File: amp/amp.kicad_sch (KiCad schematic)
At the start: 82 parts, among them J1 HI Input, J2 Speaker 8Ω, J3 Headphones, J4 LO Input, J6 FX Send, J7 FX Return, Q1 S8050, SW1 PWR, SW2 FX Enable/Bypass, U1 TL074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

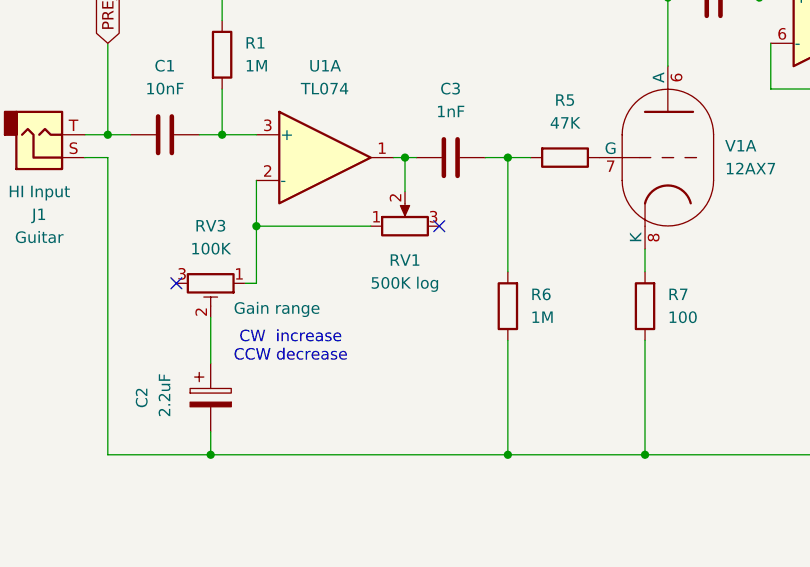
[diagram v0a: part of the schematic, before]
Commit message: Fix input opamp gain pot type (log->lin) (#38)
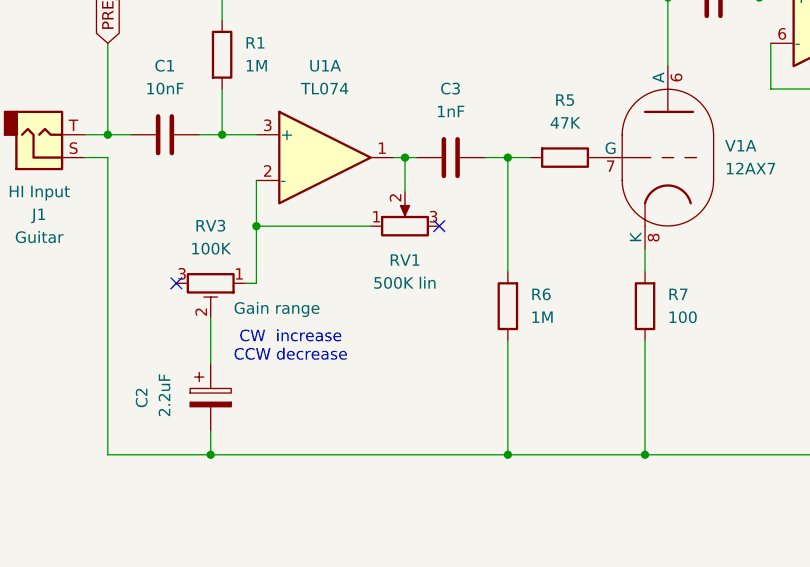
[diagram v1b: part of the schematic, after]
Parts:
- RV1: value 500K log -> 500K lin
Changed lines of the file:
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@@
 			)
 		)
-		(property "Value" "500K log"
+		(property "Value" "500K lin"
 			(at 71.12 165.1 90)
 			(effects

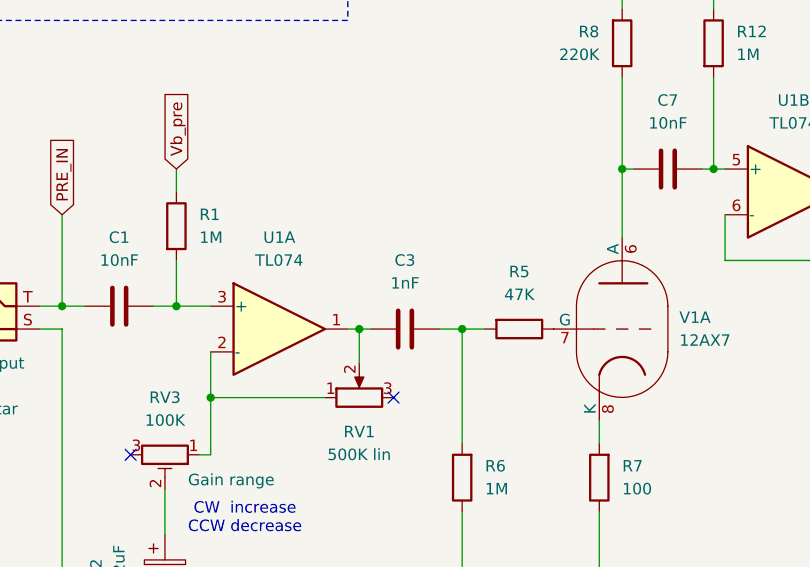
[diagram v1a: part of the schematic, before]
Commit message: u1a out coupling pot 1->10nF
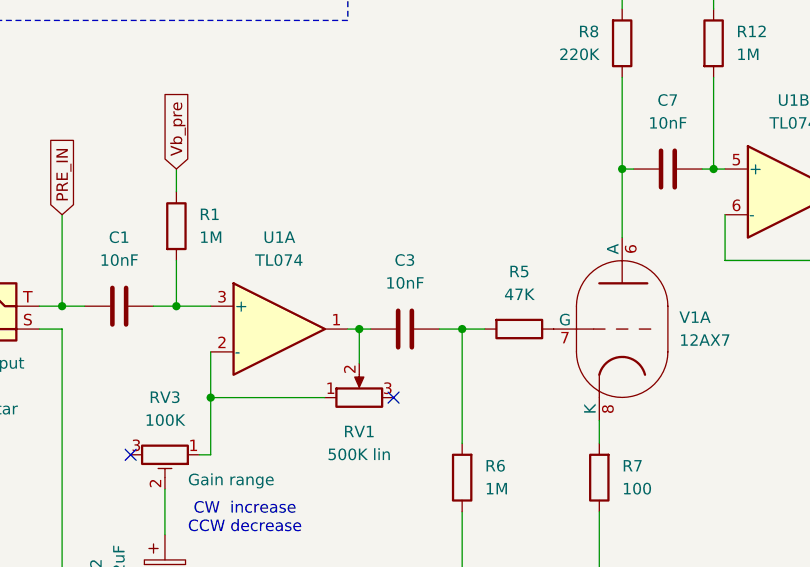
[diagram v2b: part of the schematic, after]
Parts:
- C3: value 1nF -> 10nF
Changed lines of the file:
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@@
 			)
 		)
-		(property "Value" "1nF"
+		(property "Value" "10nF"
 			(at 76.2 146.05 90)
 			(effects

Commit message: Move opamp bias source to power section
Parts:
- removed C16, C26: 10nF, symbol Device:C
- removed C25, C4: 10uF, symbol Device:C_Polarized
- removed R13, R24, R3, R4: 10K, symbol Device:R
- removed RV4, RV5: 10k, symbol Device:R_Potentiometer_Trim
- added C22: 10uF, symbol Device:C_Polarized
- added C23: 10nF, symbol Device:C
- added R22, R36: 10K, symbol Device:R
- added RV6: 10k, symbol Device:R_Potentiometer_Trim
- C14: value 100nF -> 10nF
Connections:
- net Vb_pre is gone; now on net V_{bias}: R1.1, R12.1, R14.1, R23.2
- net GND: now also R36.2
- net VCC: now also R22.2
- net Vb_mix renamed V_{bias}
- net V_{bias}: now also C22.1, C22.2, C23.1, C23.2, R22.1, RV6.2
- new net: R36.1, RV6.1
- no-connect marks 14 -> 13
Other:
- moved on the sheet: C14, C15, C6, R23, U1E, U6B

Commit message: Replace 2xNE5532 with 1xTL074
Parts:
- removed U5, U6: NE5532, symbol Amplifier_Operational:NE5532
- added C24: 10nF, symbol Device:C
- added U7: TL074, symbol Amplifier_Operational:TL074
- C27: value 1uF -> 10uF
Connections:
- net GND: now also C24.1, U7.11 (V-)
- net VCC: now also C24.2, U7.4 (V+)
- net V_{bias}: now also U7.10 (+), U7.12 (+), U7.3 (+), U7.5 (+)
- net at R32.2, R33.1, R34.1: now also U7.9 (-)
- net at C30.1, R31.1: now also U7.7
- net at R29.1, R30.1, R31.2: now also U7.6 (-)
- net at C31.1, R26.1: now also U7.1
- net at R26.2, R27.1, R28.1: now also U7.2 (-)
- net at C32.1, R32.1: now also U7.8
- new net: U7.13 (-), U7.14

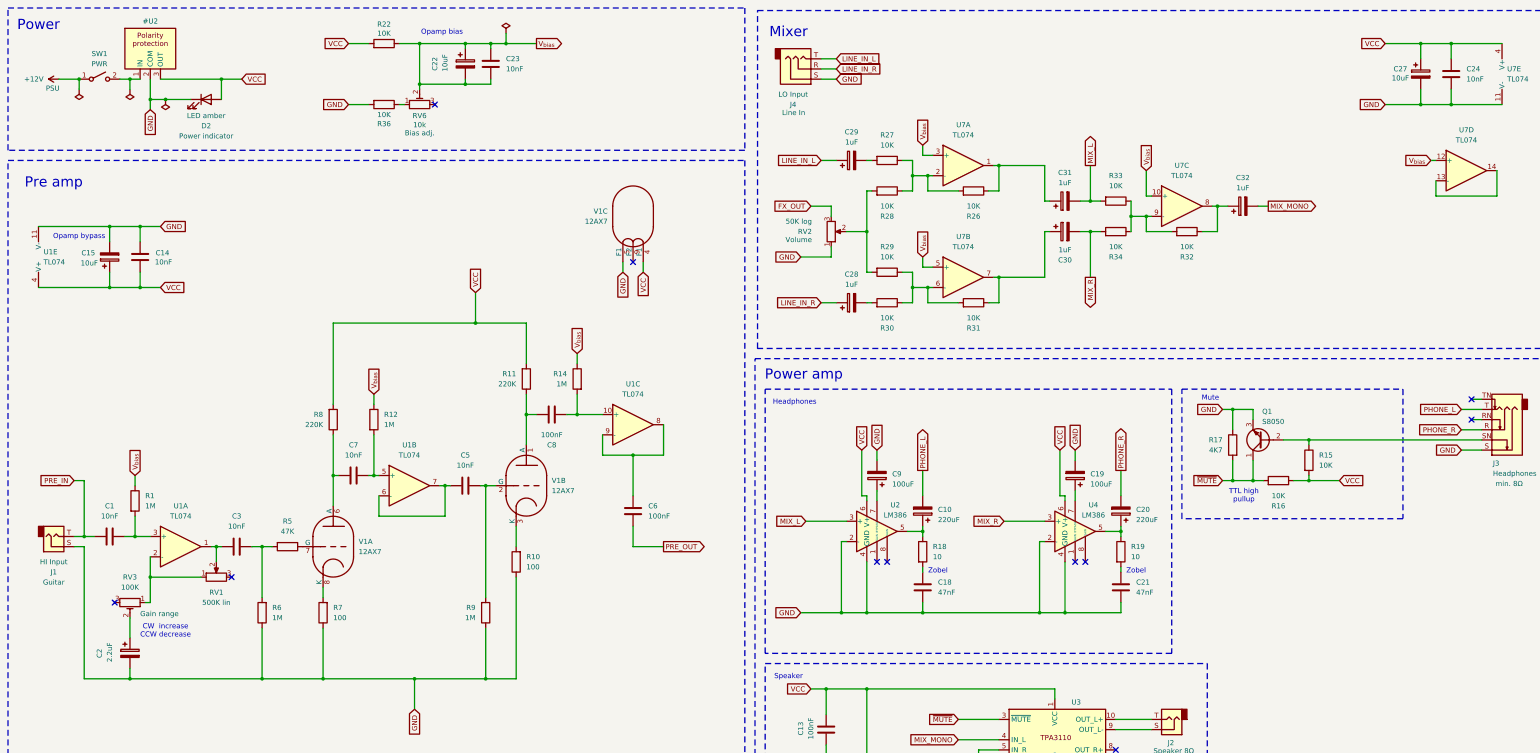
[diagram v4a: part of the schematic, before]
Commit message: Improve tube biasing (#49)
Try out Tube Cricket style tube biasing

https://beavisaudio.com/projects/TubeCricket/
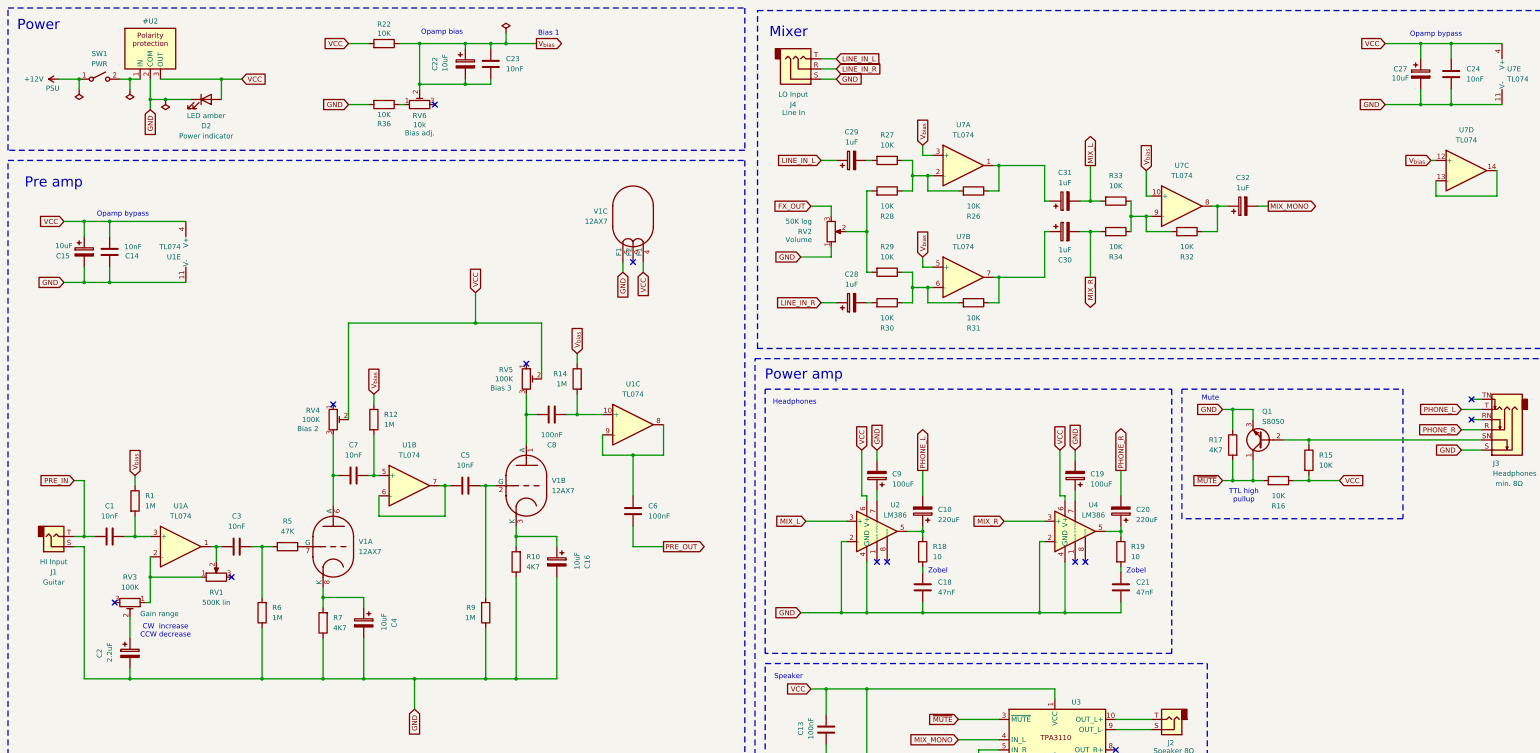
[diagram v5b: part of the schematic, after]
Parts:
- removed R11, R8: 220K, symbol Device:R
- added C16, C4: 10uF, symbol Device:C_Polarized
- added RV4, RV5: 100K, symbol Device:R_Potentiometer_Trim
- R10, R7: value 100 -> 4K7
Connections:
- net GND: now also C16.2, C4.2
- net VCC: now also RV4.2, RV5.2
- net at C8.1, V1.1 (A): now also RV5.3
- net at R7.2, V1.8 (K): now also C4.1
- net at R10.2, V1.3 (K): now also C16.1
- net at C7.1, V1.6 (A): now also RV4.3
- no-connect marks 13 -> 15
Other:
- note added: "Bias 1"
- moved on the sheet: C14, C15, R7, U1E

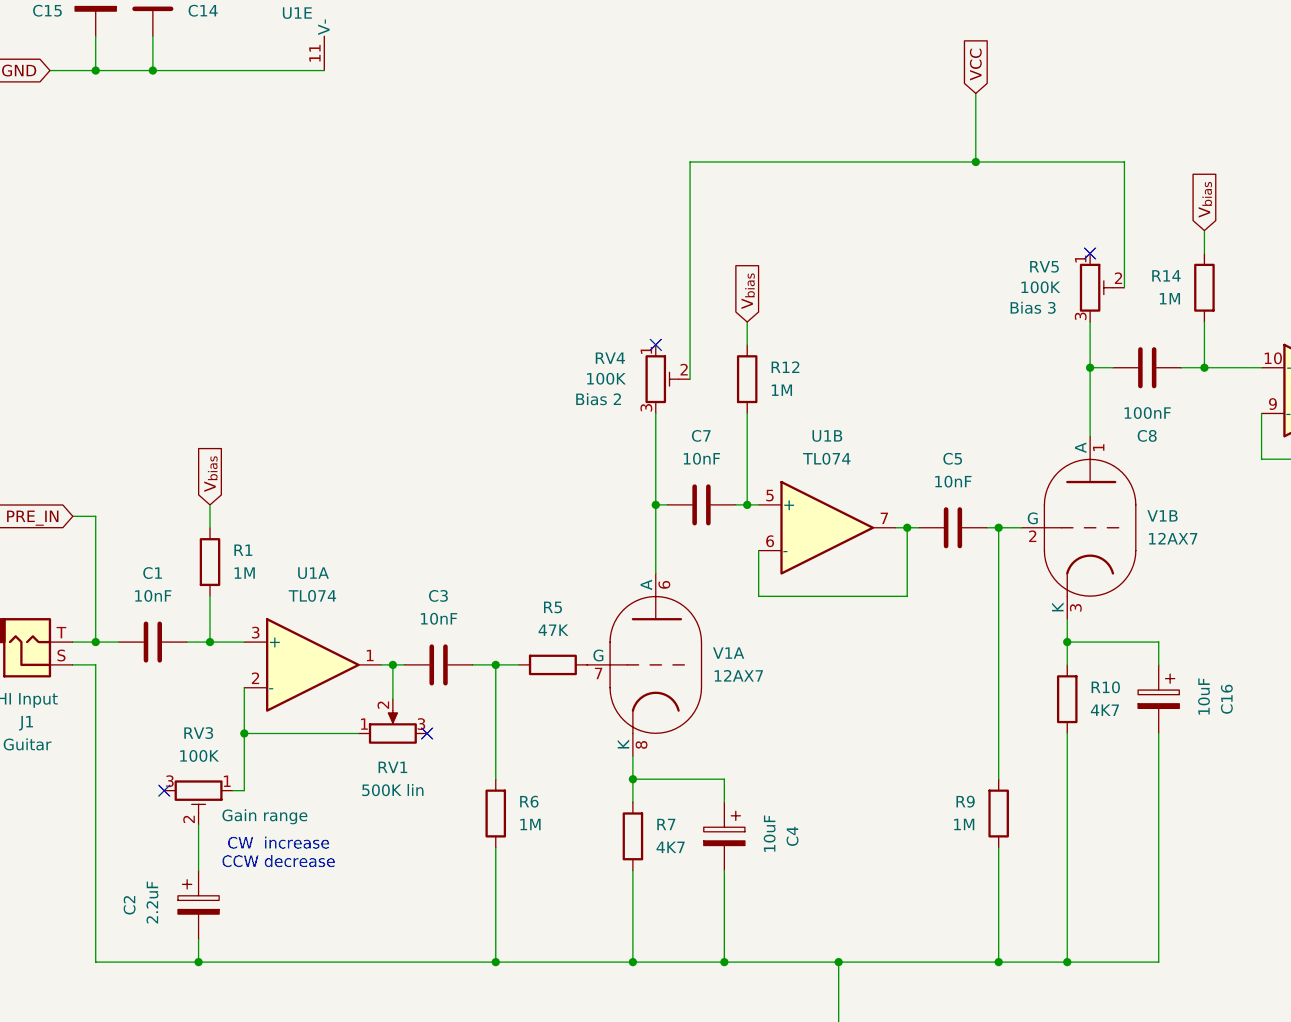
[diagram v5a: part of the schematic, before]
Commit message: Fix tube biasing
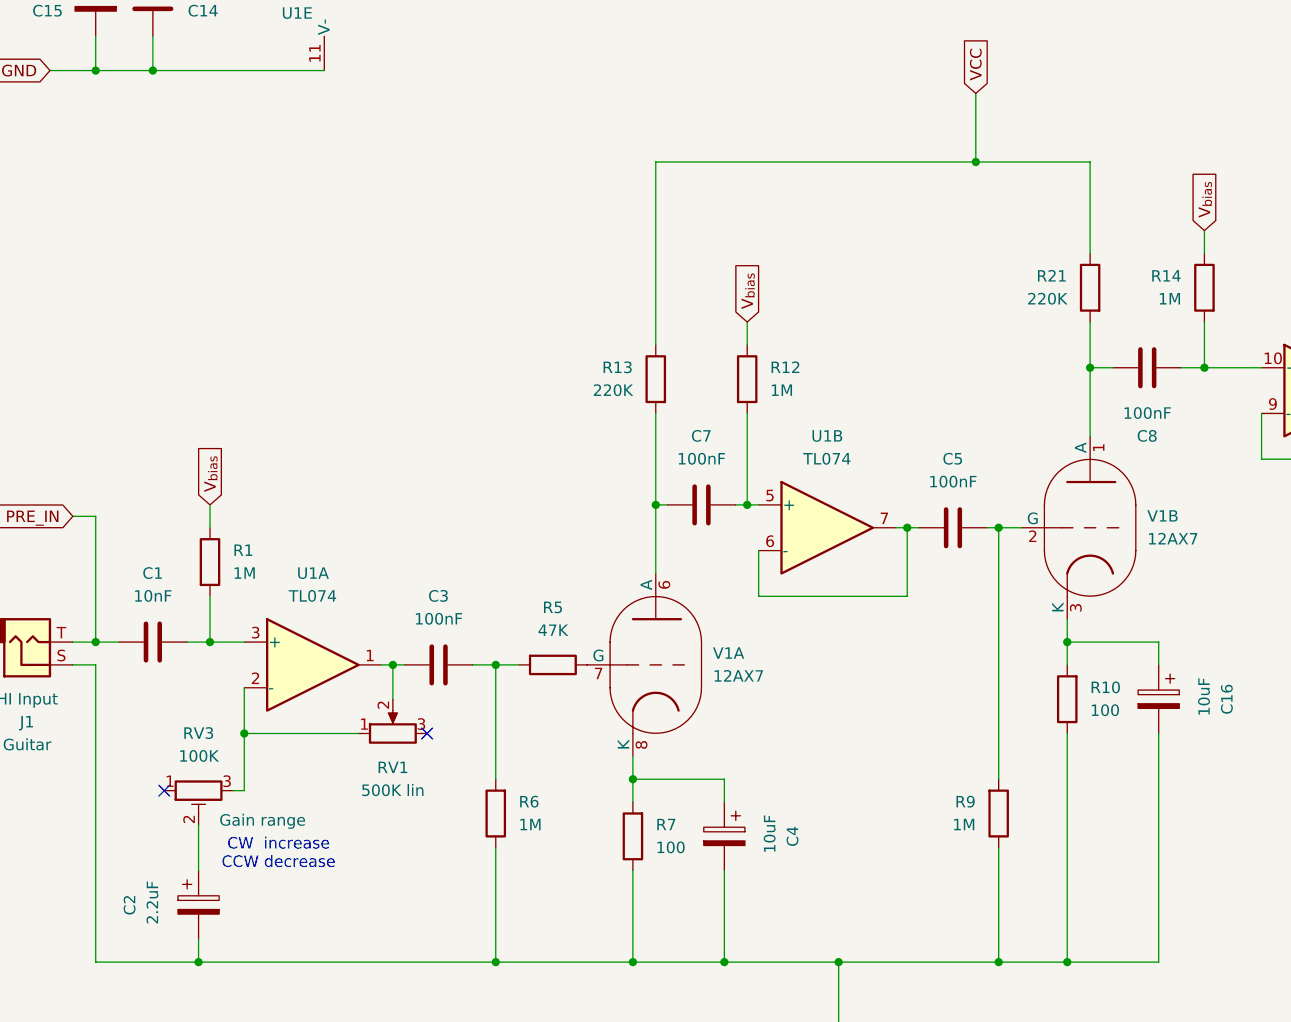
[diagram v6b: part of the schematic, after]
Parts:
- removed RV4, RV5: 100K, symbol Device:R_Potentiometer_Trim
- added R13, R21: 220K, symbol Device:R
- C3, C5, C7: value 10nF -> 100nF
- R10, R7: value 4K7 -> 100
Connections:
- net VCC: now also R13.1, R21.1
- net at C8.1, V1.1 (A): now also R21.2
- net at RV1.1, U1.2 (-): now also RV3.3; no longer RV3.1
- net at C7.1, V1.6 (A): now also R13.2
- no-connect marks 15 -> 13
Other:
- moved on the sheet: RV3
